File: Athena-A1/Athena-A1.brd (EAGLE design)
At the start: 33 x 55.1 mm, 80 parts, among them J1 MF-CON-MICROUSB-RIGHT, J2 TC2030-IDC-NL, J3 MF-CON-2.54mm-01x08, J4 MF-CON-2.54mm-01x08, J5 MF-CON-2.54mm-01x07, SW1 MF-SW-TACT-6MM, SW2 MF-SW-TACT-6MM, U1 PRTR5V0U2X,215, U2 MCP73831T-2ACI/OT, U3 AP2112K-3.3TRG1, U4 RT9080-18GJ5, U5 MK22FN128VLH10, U6 FE310, U7 32MBit, X1 JST 2-Pin, Y1 TSX-3225-16.0000MF18X-AC0, Y2 KX3211A0032.768000

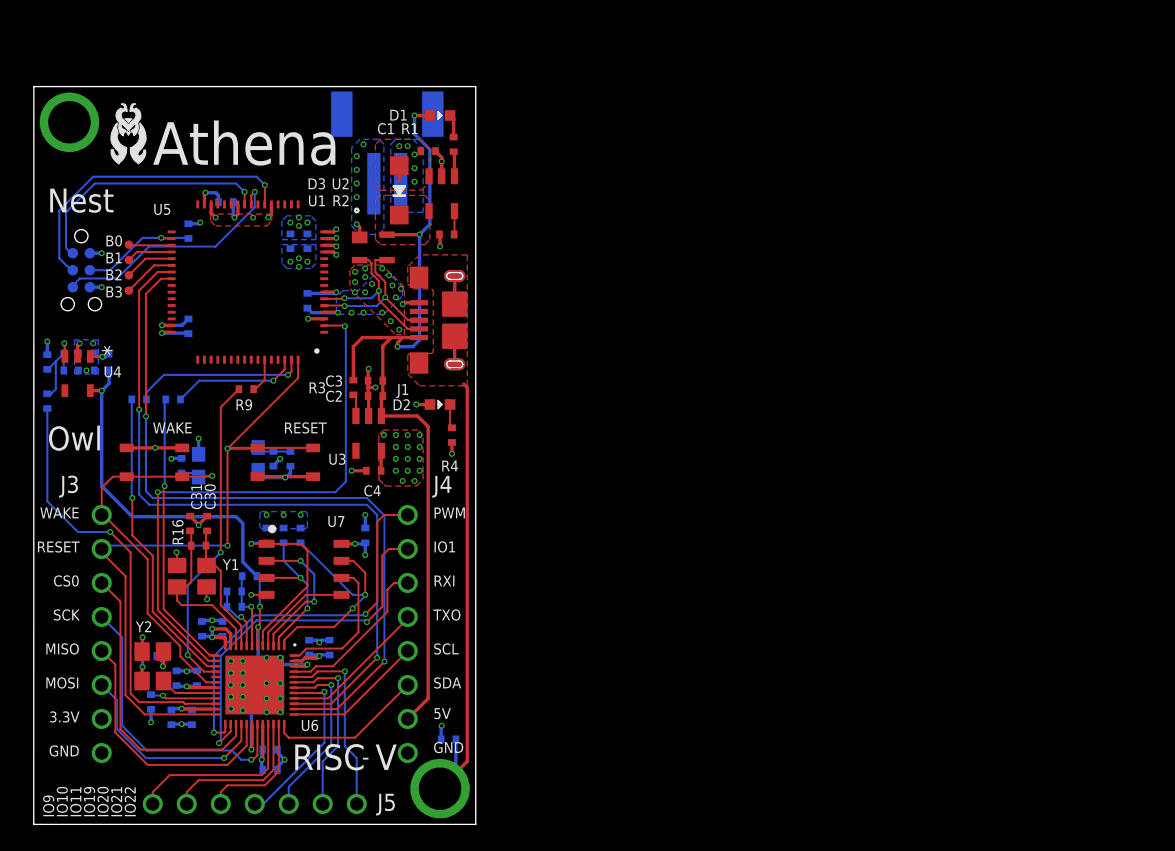
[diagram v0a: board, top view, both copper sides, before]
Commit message: Updates post-review in progress
Sch: added power switch, improved symbols, added cap on Wake, added 0Ohm res to crystal, mikro gpio instead of wake/reset

Brd: moved tag connect to top, added clearance for mikro click brds, routed new switch, etc.

Todo: silkscreen cleanup and checking
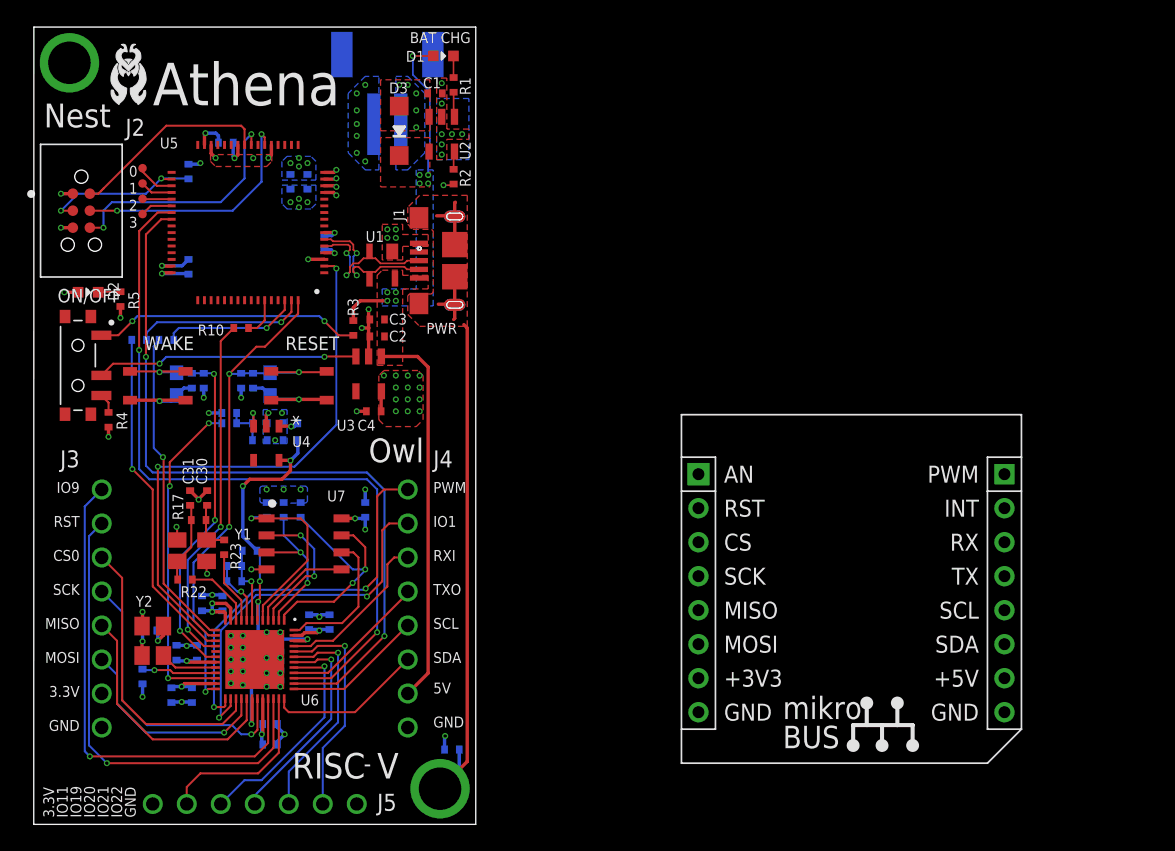
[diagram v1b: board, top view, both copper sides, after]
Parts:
- removed B0, B1, B2, B3: TPB0,65, Athena-r1p0:TP_B0,65
- added 0, 1, 2, 3: TPB0,65, Athena-A1:TP_B0,65
- added C33: 0.1uF, Athena-A1:C0402
- added ON/OFF: PCM12SMTR, Athena-A1:SW_PCM12SMTR
- added R21: 10, Athena-A1:R0402
- added R22, R23: 0, Athena-A1:R0402
- added X2: MIKROE_CLICKMINI, OSDZU3_ref_dsn:MIKROE_BUS_MINI
- C1, C10, C11, C12, C13, C14, C15, C16, C17, C18, C19, C2, C20, C21, C22, C23, C24, C25, C26, C27, C28, C3, C30, C31, C32, C4, C5, C6, C7, C8, C9: device Athena-r1p0:C0402 -> Athena-A1:C0402
- C29: value 0.1uF -> 0.01uF; device Athena-r1p0:C0402 -> Athena-A1:C0402
- D1, D2: device Athena-r1p0:LED0603 -> Athena-A1:LED0603
- D3: device Athena-r1p0:SOD-123 -> Athena-A1:SOD-123
- D4, D5: device Athena-r1p0:TVS0603 -> Athena-A1:TVS0603
- J1: device Athena-r1p0:MICROUSB-RIGHT -> Athena-A1:MICROUSB-RIGHT
- J2: device Athena-r1p0:TAG_TC2030-IDC-NL -> Athena-A1:TAG_TC2030-IDC-NL
- J3, J4: device Athena-r1p0:PTH_2.54MM_01X08 -> Athena-A1:PTH_2.54MM_01X08
- J5: device Athena-r1p0:PTH_2.54MM_01X07 -> Athena-A1:PTH_2.54MM_01X07
- MGT1, MGT2: device Athena-r1p0:MOUNTING_HOLE -> Athena-A1:MOUNTING_HOLE
- R1, R10, R11, R12, R14, R15, R18, R19, R2, R3, R7: device Athena-r1p0:R0402 -> Athena-A1:R0402
- R13: value 100k -> 100; device Athena-r1p0:R0402 -> Athena-A1:R0402
- R16: value 1M -> 100k; device Athena-r1p0:R0402 -> Athena-A1:R0402
- R17: value 100k -> 1M; device Athena-r1p0:R0402 -> Athena-A1:R0402
- R20: value 10 -> 100k; device Athena-r1p0:R0402 -> Athena-A1:R0402
- R4: value 1k -> 100k; device Athena-r1p0:R0402 -> Athena-A1:R0402
- R5: value 100k -> 1k; device Athena-r1p0:R0402 -> Athena-A1:R0402
- R6: value DNP -> 100k; device Athena-r1p0:R0402 -> Athena-A1:R0402
- R8: value 100k -> DNP; device Athena-r1p0:R0402 -> Athena-A1:R0402
- R9: value 100 -> 100k; device Athena-r1p0:R0402 -> Athena-A1:R0402
- SW1, SW2: device Athena-r1p0:TACT4.2MM -> Athena-A1:TACT4.2MM
- U1: device Athena-r1p0:SOT143B_PRTR5V0U2X,215_NEX -> Athena-A1:SOT143B_PRTR5V0U2X,215_NEX
- U2, U3: device Athena-r1p0:SOT23-5 -> Athena-A1:SOT23-5
- U4: device Athena-r1p0:TSOT23-5_ONS -> Athena-A1:TSOT23-5_ONS
- U5: device Athena-r1p0:IC_USB_JTAG_LQFP-64 -> Athena-A1:IC_USB_JTAG_LQFP-64
- U6: device Athena-r1p0:MCU_QFN-48-.4MMPITCH -> Athena-A1:MCU_QFN-48-.4MMPITCH
- U7: device Athena-r1p0:IC-MEMORY_SO08 -> Athena-A1:IC-MEMORY_SO08
- X1: device Athena-r1p0:JSTPH2 -> Athena-A1:JSTPH2
- Y1, Y2: device Athena-r1p0:SMD-4 -> Athena-A1:SMD-4
- moved D2 27.6 mm to (4.06, 39.8)
- moved R4 25.7 mm to (5.59, 30.2)
- moved R20 21.9 mm to (17.4, 23.5), turned to 270 degrees
- moved C29 20.8 mm to (11.8, 33.1), turned to 270 degrees
- moved R12 19.5 mm to (7.87, 36.2), turned to 180 degrees
- moved C32 17.6 mm to (8.64, 14.5), turned to 0 degrees
- moved R9 16.8 mm to (11.6, 48.8), flipped to the bottom, turned to 270 degrees
- moved R8 16.5 mm to (16.9, 28.7), turned to 0 degrees
- moved C5 15.0 mm to (19.2, 30.0)
- moved C7 15.0 mm to (16.9, 30.0)
- moved C6 15.0 mm to (19.2, 28.7)
- moved U4 15.0 mm to (17.4, 28.5)
- moved R6 14.3 mm to (14.6, 30.0), turned to 180 degrees
- moved R16 12.7 mm to (15.5, 33.1), flipped to the bottom, turned to 90 degrees
- moved R7 12.2 mm to (14.6, 30.7)
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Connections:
- removed net IO10: J5.P$2, U6.34
- new net N$16: ON/OFF.2, U3.3
- new net N$17: ON/OFF.3, R4.P$1
- new net N$18: C30.P$1, R17.P$1, R23.P$2, Y1.1
- new net N$19: C31.P$1, R17.P$2, R22.P$1, Y1.3
- new net RST: J3.P$2, U6.34
- net 1.8V: now also R13.P$1; no longer R12.P$1
- net 16MHZ_IN: now also R23.P$1; no longer C30.P$1, R16.P$1, Y1.1
- net 16MHZ_OUT: now also R22.P$2; no longer C31.P$1, R16.P$2, Y1.3
- net 3.3V: now also C33.P$1, J5.P$1, R16.P$1, R20.P$1, R7.P$2, R9.P$1; no longer C29.P$1, R13.P$1, R17.P$1, R6.P$2, R8.P$1
- net CGND: now also R21.P$1; no longer R20.P$1
- net DBG_RESET: now also R9.P$2; no longer R8.P$2
- net GND: now also C33.P$2, J5.P$7, R21.P$2, R5.P$2, R8.P$1; no longer R20.P$2, R7.P$1
- net IO11: now also J5.P$2; no longer J5.P$3
- net IO19: now also J5.P$3; no longer J5.P$4
- net IO20: now also J5.P$4; no longer J5.P$5
- net IO21: now also J5.P$5; no longer J5.P$6
- net IO22: now also J5.P$6; no longer J5.P$7
- net IO9: now also J3.P$1; no longer J5.P$1
- net JTAG_TCK: now also R11.P$2; no longer R10.P$2
- net JTAG_TDI: now also R10.P$2; no longer R9.P$2
- net JTAG_TMS: now also R12.P$1; no longer R11.P$1
- net N$1: now also ON/OFF.1; no longer U3.3
- net N$11: now also R10.P$1; no longer R9.P$1
- net N$12: now also 0.TP; no longer B0.TP
- net N$13: now also 1.TP; no longer B1.TP
- net N$14: now also 2.TP; no longer B2.TP
- net N$15: now also 3.TP; no longer B3.TP
- net N$2: now also R5.P$1; no longer R4.P$1
- net N$4: now also R6.P$2, R7.P$1, R8.P$2; no longer R5.P$2, R6.P$1, R7.P$2
- net N$8: now also R12.P$2; no longer R11.P$2
- net N$9: now also R11.P$1; no longer R10.P$1
- net PLL_AVDD: now also R13.P$2; no longer R12.P$2
- net QSPI_CS: now also R20.P$2; no longer R19.P$2
- net QSPI_DQ2: now also R18.P$2; no longer R17.P$2
- net QSPI_DQ3: now also R19.P$2; no longer R18.P$2
- net RESET: now also R16.P$2; no longer J3.P$2, R14.P$2
- net USB_N: now also U1.3; no longer U1.2
- net USB_P: now also U1.2; no longer U1.3
- net VDD_CORE_EN: now also R6.P$1; no longer R5.P$1
- net WAKE: now also C29.P$1, R14.P$2; no longer J3.P$1, R13.P$2
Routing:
- net RST: track 0.00 -> 35.5 mm, vias 0 -> 1
- net IO9: track 13.6 -> 37.7 mm, vias 0 -> 1
- net V_USB: track 64.0 -> 43.6 mm, vias 3 -> 9
- net N$16: track 0.00 -> 19.6 mm, vias 0 -> 2
- net N$1: track 1.66 -> 20.0 mm, vias 0 -> 2
- net 1.8V: track 47.3 -> 34.2 mm, vias 5 -> 6
- net RESET: track 55.8 -> 43.5 mm, vias 2 -> 4
- net IO10: track 11.5 -> 0.00 mm
- net CGND: track 40.9 -> 49.5 mm
- net 16MHZ_OUT: track 12.6 -> 5.26 mm
- net VDD_CORE_EN: track 31.9 -> 24.8 mm, vias 1 -> 3
- net N$19: track 0.00 -> 6.04 mm
- net DBG_SWDCLK: track 23.1 -> 18.2 mm, vias 1 -> 2
- net 16MHZ_IN: track 10.1 -> 5.44 mm
- net N$18: track 0.00 -> 3.95 mm
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- added copper zone on layer 16, net V_USB
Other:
- board size 33 x 55.1 mm -> 33 x 59.6 mm
- board text added: "BAT CHG"
- board text added: "PWR"
- board text added: "RST"
- board text removed: "IO10"

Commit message: Finished updates post-review
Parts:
- moved R3 16.9 mm to (6.99, 36.1), turned to 270 degrees
- moved X2 9.80 mm to (57.8, 1.78)
- moved R12 8.89 mm to (16.8, 36.4), flipped to the top, turned to 0 degrees
- moved R11 6.93 mm to (16.8, 37.2), flipped to the top, turned to 180 degrees
- moved R10 1.55 mm to (16.8, 38.0)
- moved D2 1.42 mm to (2.67, 39.5)
- moved R5 1.30 mm to (5.21, 39.5), turned to 0 degrees
- moved J2 1.14 mm to (3.56, 47.0)
- moved R7 1.09 mm to (15.5, 30.1), turned to 270 degrees
- moved R6 0.85 mm to (15.0, 30.7), flipped to the top, turned to 0 degrees
- moved R15 0.25 mm to (8.13, 10.8)
- moved C32 0.13 mm to (8.64, 14.4)
- moved Y2 0.13 mm to (8.89, 13.6)
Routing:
- net N$1: track 20.0 -> 1.95 mm, vias 2 -> 0
- net V_USB: track 43.6 -> 60.8 mm
- net JTAG_TDI: track 26.6 -> 35.6 mm
- net N$8: track 12.9 -> 4.01 mm, vias 1 -> 0
- net JTAG_TCK: track 24.0 -> 32.6 mm, vias 1 -> 2
- net N$9: track 10.2 -> 3.04 mm, vias 1 -> 0
- net JTAG_TMS: track 25.4 -> 32.2 mm, vias 1 -> 2
- net VDD_CORE_EN: track 24.8 -> 28.2 mm, vias 3 -> 2
- net UART_RX_MK22: track 57.5 -> 59.9 mm, vias 2 -> 4
- net UART_TX_MK22: track 57.4 -> 59.7 mm, vias 2 -> 4
- net N$11: track 2.95 -> 1.21 mm
- net RESET: track 43.5 -> 44.8 mm, vias 4 -> 3
- net JTAG_TDO: track 42.0 -> 42.7 mm
- net 1.8V: track 34.2 -> 34.5 mm, vias 6 -> 5
- net WAKE: track 32.1 -> 32.2 mm, vias 4 -> 3
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
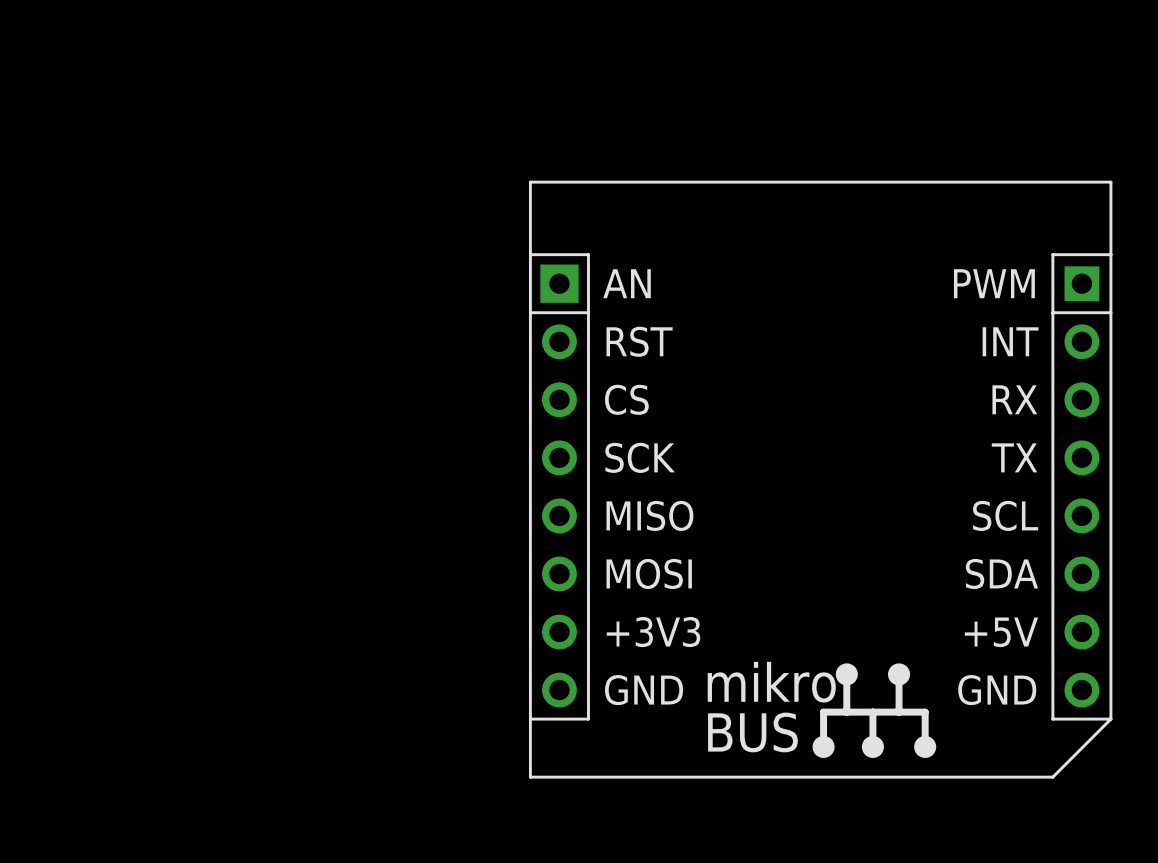
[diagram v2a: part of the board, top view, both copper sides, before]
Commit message: Moved pours outside dimension
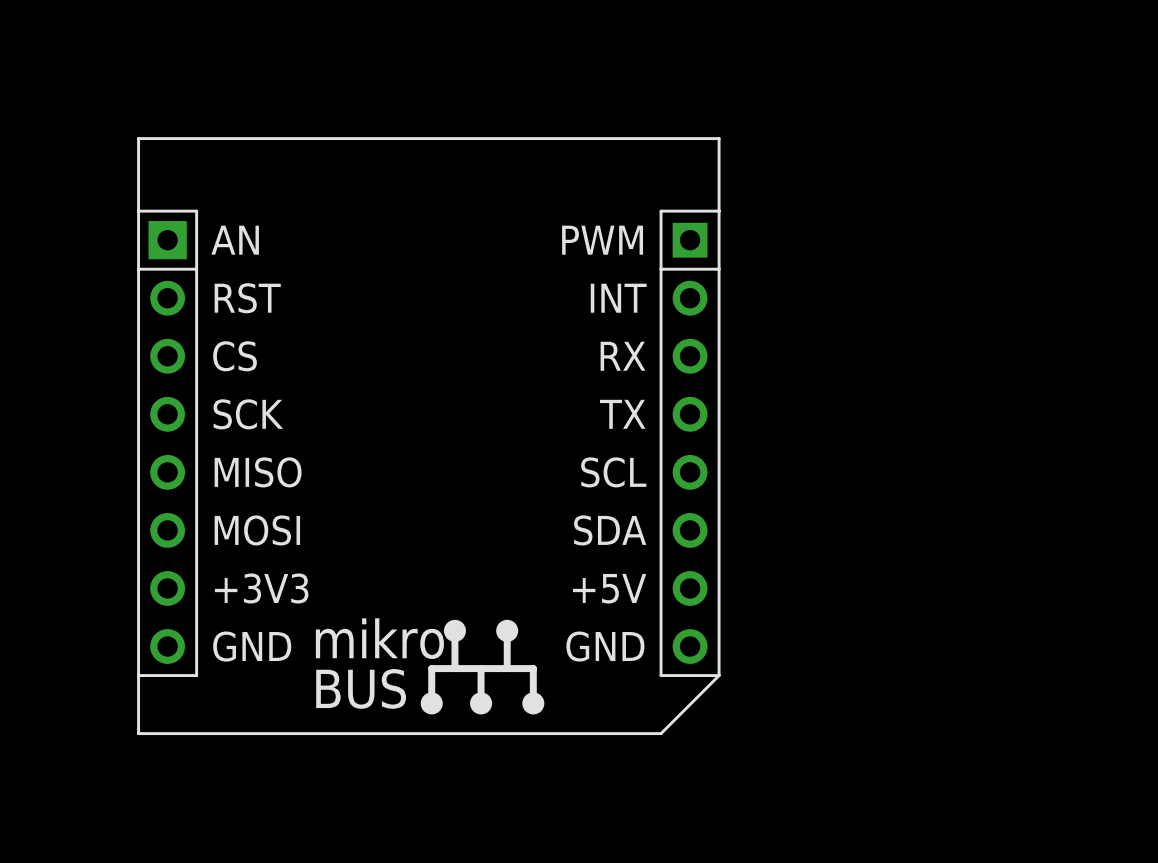
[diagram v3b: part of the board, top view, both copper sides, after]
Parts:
- moved X2 17.3 mm to (40.6, 3.68)
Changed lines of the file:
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@@
 <grid distance="5" unitdist="mil" unit="mil" style="lines" multiple="1" display="yes" altdistance="1" altunitdist="mil" altunit="mil"/>
 <layers>
-<layer number="1" name="Top" color="4" fill="1" visible="yes" active="yes"/>
-<layer number="2" name="Route2" color="16" fill="1" visible="no" active="yes"/>
+<layer number="1" name="Top" color="4" fill="1" visible="no" active="yes"/>
+<layer number="2" name="Route2" color="16" fill="1" visible="yes" active="yes"/>
 <layer number="3" name="Route3" color="17" fill="1" visible="no" active="no"/>
 <layer number="4" name="Route4" color="18" fill="1" visible="no" active="no"/>
@@
 <layer number="13" name="Route13" color="21" fill="1" visible="no" active="no"/>
 <layer number="14" name="Route14" color="22" fill="1" visible="no" active="no"/>
-<layer number="15" name="Route15" color="23" fill="1" visible="no" active="yes"/>
-<layer number="16" name="Bottom" color="1" fill="1" visible="no" active="yes"/>
+<layer number="15" name="Route15" color="23" fill="1" visible="yes" active="yes"/>
+<layer number="16" name="Bottom" color="1" fill="1" visible="yes" active="yes"/>
 <layer number="17" name="Pads" color="2" fill="1" visible="yes" active="yes"/>
 <layer number="18" name="Vias" color="2" fill="1" visible="yes" active="yes"/>
 <layer number="19" name="Unrouted" color="6" fill="1" visible="yes" active="yes"/>
 <layer number="20" name="Dimension" color="24" fill="1" visible="yes" active="yes"/>
-<layer number="21" name="tPlace" color="7" fill="1" visible="yes" active="yes"/>
-<layer number="22" name="bPlace" color="7" fill="1" visible="no" active="yes"/>
-<layer number="23" name="tOrigins" color="15" fill="1" visible="yes" active="yes"/>
-<layer number="24" name="bOrigins" color="15" fill="1" visible="no" active="yes"/>
-<layer number="25" name="tNames" color="7" fill="1" visible="yes" active="yes"/>
-<layer number="26" name="bNames" color="7" fill="1" visible="no" active="yes"/>
+<layer number="21" name="tPlace" color="7" fill="1" visible="no" active="yes"/>
+<layer number="22" name="bPlace" color="7" fill="1" visible="yes" active="yes"/>
+<layer number="23" name="tOrigins" color="15" fill="1" visible="no" active="yes"/>
+<layer number="24" name="bOrigins" color="15" fill="1" visible="yes" active="yes"/>
+<layer number="25" name="tNames" color="7" fill="1" visible="no" active="yes"/>
+<layer number="26" name="bNames" color="7" fill="1" visible="yes" active="yes"/>
 <layer number="27" name="tValues" color="7" fill="1" visible="no" active="yes"/>
 <layer number="28" name="bValues" color="7" fill="1" visible="no" active="yes"/>
@@
 <attribute name="PRICE" value="None" x="15.29715" y="57.81675" size="1.778" layer="27" rot="R270" display="off"/>
 </element>
-<element name="X2" library="OSDZU3_ref_dsn" package="MIKROE_BUS_MINI" value="MIKROE_CLICKMINI" x="57.785" y="1.778" smashed="yes"/>
+<element name="X2" library="OSDZU3_ref_dsn" package="MIKROE_BUS_MINI" value="MIKROE_CLICKMINI" x="40.64" y="3.683" smashed="yes"/>
 <element name="ON/OFF" library="Athena-A1" package="SW_PCM12SMTR" value="PCM12SMTR" x="3.302" y="34.29" smashed="yes" rot="R270">
 <attribute name="DESCRIPTION" value=" Slide Switch SPDT Surface Mount, Right Angle " x="3.302" y="34.29" size="1.778" layer="27" rot="R270" display="off"/>
@@
 <contactref element="J3" pad="P$7"/>
 <polygon width="0.1524" layer="15">
-<vertex x="0.762" y="60.198"/>
-<vertex x="32.258" y="60.198"/>
-<vertex x="32.258" y="0.762"/>
-<vertex x="0.762" y="0.762"/>
+<vertex x="-0.762" y="60.198"/>
+<vertex x="33.782" y="60.198"/>
+<vertex x="33.782" y="-0.889"/>
+<vertex x="-0.762" y="-0.889"/>
 </polygon>
 <via x="17.0302" y="6.731" extent="1-16" drill="0.254"/>
@@
 <contactref element="R21" pad="P$2"/>
 <polygon width="0.1524" layer="2">
-<vertex x="0.762" y="60.198"/>
-<vertex x="32.258" y="60.198"/>
-<vertex x="32.258" y="0.762"/>
-<vertex x="0.762" y="0.762"/>
+<vertex x="-1.524" y="61.087"/>
+<vertex x="34.544" y="61.087"/>
+<vertex x="34.544" y="-1.651"/>
+<vertex x="-1.524" y="-1.651"/>
 </polygon>
 <via x="11.049" y="9.144" extent="1-16" drill="0.254"/>

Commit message: Athena A1 final
Minor board cleanup
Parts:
- removed X2: MIKROE_CLICKMINI, OSDZU3_ref_dsn:MIKROE_BUS_MINI
- renumbered ON/OFF to SW3
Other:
- board text added: "OFF"
- board text added: "ON"
